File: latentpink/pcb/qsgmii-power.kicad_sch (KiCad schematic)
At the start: 169 parts, among them U1 VSC8512

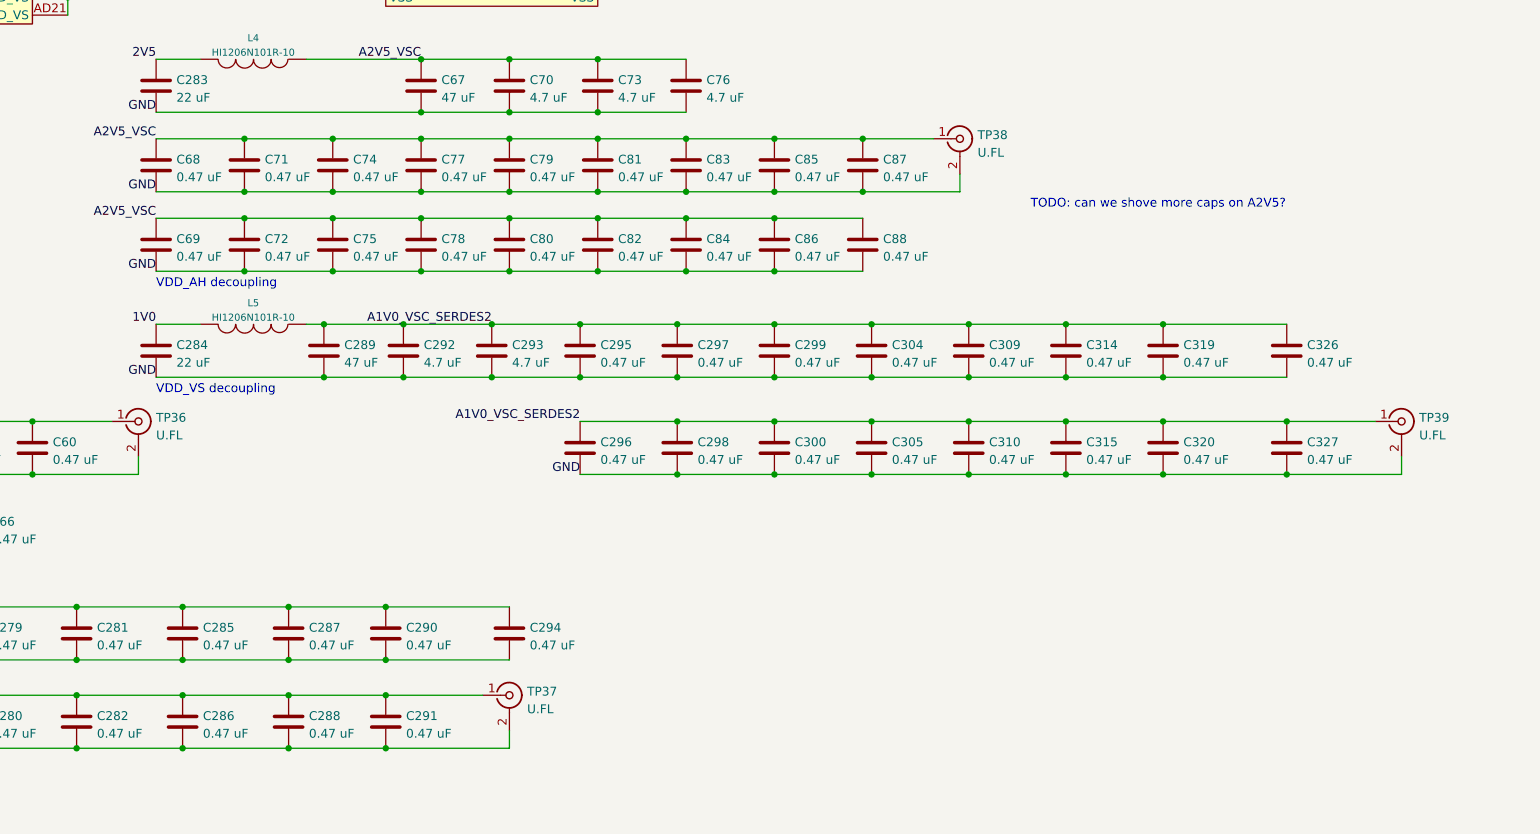
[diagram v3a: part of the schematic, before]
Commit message: Updated schematic with notes on power rail sequencing bug found during bringup
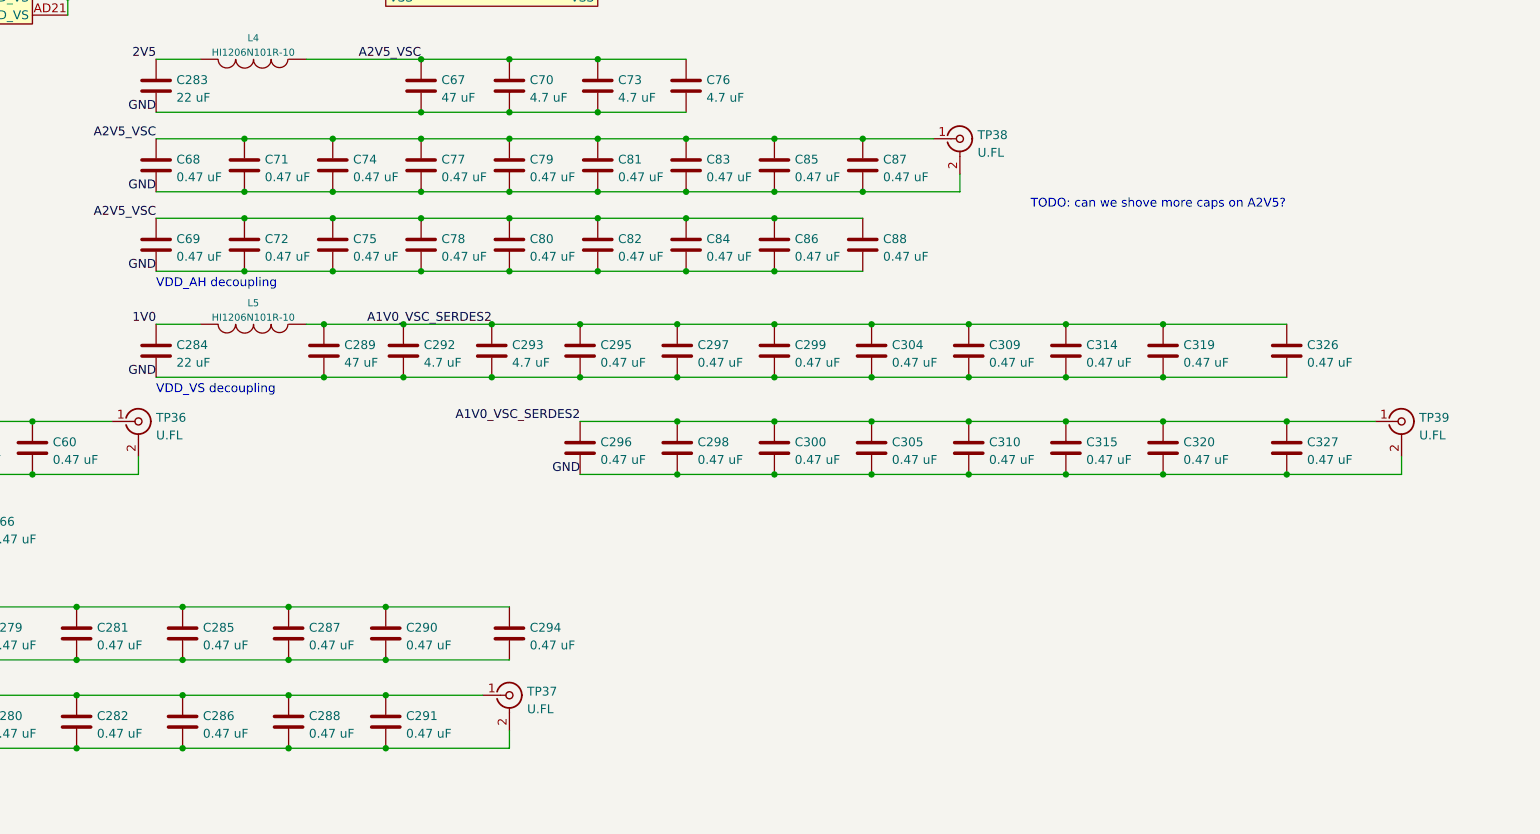
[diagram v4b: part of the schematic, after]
